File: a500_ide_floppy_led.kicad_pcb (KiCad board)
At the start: 2 copper layers, 21.3 x 11.8 mm, 6 parts, among them J1 Motherboard, J2 Keyboard, J3 ~{IDE_ACTIVITY}, Q1 2N3906

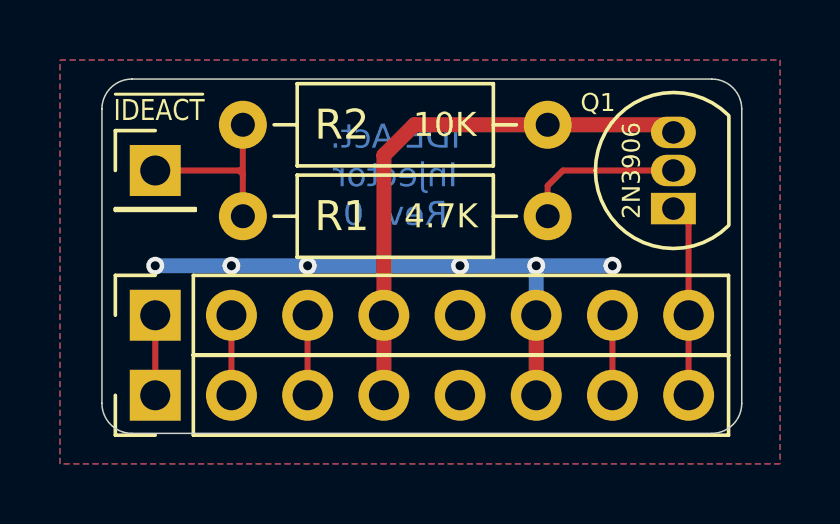
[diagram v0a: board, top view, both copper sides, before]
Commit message: Slightly shrink the board
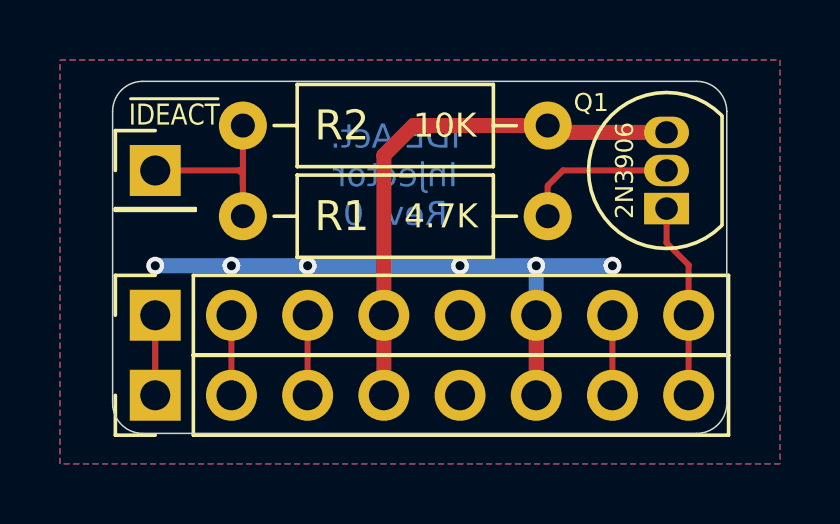
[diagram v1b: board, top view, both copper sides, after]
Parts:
- moved Q1 0.23 mm to (119.3, 25.3)
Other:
- board size 21.3 x 11.8 mm -> 20.5 x 11.7 mm
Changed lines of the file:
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@@
 	(footprint "Resistor_THT:R_Axial_DIN0207_L6.3mm_D2.5mm_P10.16mm_Horizontal"
 		(layer "F.Cu")
-		(at 115.316 22.479 180)
+		(at 115.316 22.5044 180)
 		(descr "Resistor, Axial_DIN0207 series, Axial, Horizontal, pin pitch=10.16mm, 0.25W = 1/4W, length*diameter=6.3*2.5mm^2, http://cdn-reichelt.de/documents/datenblatt/B400/1_4W%23YAG.pdf")
 		(tags "Resistor Axial_DIN0207 series Axial Horizontal pin pitch 10.16mm 0.25W = 1/4W length 6.3mm diameter 2.5mm")
@@
 	(footprint "Package_TO_SOT_THT:TO-92_Inline"
 		(layer "F.Cu")
-		(at 119.507 25.273 90)
+		(at 119.2784 25.273 90)
 		(descr "TO-92 leads in-line, narrow, oval pads, drill 0.75mm (see NXP sot054_po.pdf)")
 		(tags "to-92 sc-43 sc-43a sot54 PA33 transistor")
@@
 		)
 	)
-	(gr_line
-		(start 100.457 31.766)
-		(end 100.457 21.955)
+	(gr_arc
+		(start 120.285 21.0312)
+		(mid 120.992107 21.324093)
+		(end 121.285 22.0312)
 		(stroke
 			(width 0.05)
@@
 	)
 	(gr_line
-		(start 101.457 20.955)
-		(end 120.785 20.955)
+		(start 100.8142 31.766)
+		(end 100.8142 22.0312)
 		(stroke
 			(width 0.05)
@@
 	)
 	(gr_arc
-		(start 120.785 20.955)
-		(mid 121.492107 21.247893)
-		(end 121.785 21.955)
+		(start 100.8142 22.0312)
+		(mid 101.107093 21.324093)
+		(end 101.8142 21.0312)
 		(stroke
 			(width 0.05)
@@
 		(layer "Edge.Cuts")
 	)
-	(gr_arc
-		(start 101.457 32.766)
-		(mid 100.749893 32.473107)
-		(end 100.457 31.766)
+	(gr_line
+		(start 121.285 22.0312)
+		(end 121.285 31.766)
 		(stroke
 			(width 0.05)
@@
 		(layer "Edge.Cuts")
 	)
-	(gr_arc
-		(start 121.785 31.766)
-		(mid 121.492107 32.473107)
-		(end 120.785 32.766)
+	(gr_line
+		(start 101.8142 21.0312)
+		(end 120.285 21.0312)
 		(stroke
 			(width 0.05)
@@
 		(layer "Edge.Cuts")
 	)
-	(gr_line
-		(start 120.785 32.766)
-		(end 101.457 32.766)
+	(gr_arc
+		(start 101.8142 32.766)
+		(mid 101.107093 32.473107)
+		(end 100.8142 31.766)
 		(stroke
 			(width 0.05)
@@
 		(layer "Edge.Cuts")
 	)
-	(gr_arc
-		(start 100.457 21.955)
-		(mid 100.749893 21.247893)
-		(end 101.457 20.955)
+	(gr_line
+		(start 120.285 32.766)
+		(end 101.8142 32.766)
 		(stroke
 			(width 0.05)
@@
 		(layer "Edge.Cuts")
 	)
-	(gr_line
-		(start 121.785 21.955)
-		(end 121.785 31.766)
+	(gr_arc
+		(start 121.285 31.766)
+		(mid 120.992107 32.473107)
+		(end 120.285 32.766)
 		(stroke
 			(width 0.05)
@@
 	)
 	(gr_text "~{IDEACT}"
-		(at 102.362 21.9964 0)
+		(at 102.87 22.1488 0)
 		(layer "F.SilkS")
 		(effects
@@
 	)
 	(segment
-		(start 109.855 23.495)
-		(end 110.871 22.479)
+		(start 119.2784 22.733)
+		(end 115.5446 22.733)
 		(width 0.5)
 		(layer "F.Cu")
@@
 	)
 	(segment
-		(start 110.871 22.479)
-		(end 115.316 22.479)
+		(start 115.316 22.5044)
+		(end 110.8456 22.5044)
 		(width 0.5)
 		(layer "F.Cu")
@@
 	)
 	(segment
-		(start 115.316 22.479)
-		(end 119.253 22.479)
+		(start 119.0244 22.479)
+		(end 119.2784 22.733)
+		(width 0.5)
+		(layer "F.Cu")
+		(net 1)
+	)
+	(segment
+		(start 110.8456 22.5044)
+		(end 109.855 23.495)
 		(width 0.5)
 		(layer "F.Cu")
@@
 		(start 109.855 28.829)
 		(end 109.855 23.495)
+		(width 0.5)
+		(layer "F.Cu")
+		(net 1)
+	)
+	(segment
+		(start 115.5446 22.733)
+		(end 115.316 22.5044)
 		(width 0.5)
 		(layer "F.Cu")
@@
 	)
 	(segment
-		(start 120.015 25.781)
-		(end 119.507 25.273)
-		(width 0.2)
-		(layer "F.Cu")
-		(net 8)
-	)
-	(segment
 		(start 120.015 28.829)
-		(end 120.015 25.781)
+		(end 120.015 27.1526)
 		(width 0.2)
 		(layer "F.Cu")
@@
 	)
 	(segment
+		(start 119.2784 26.416)
+		(end 119.2784 25.273)
+		(width 0.2)
+		(layer "F.Cu")
+		(net 8)
+	)
+	(segment
+		(start 120.015 27.1526)
+		(end 119.2784 26.416)
+		(width 0.2)
+		(layer "F.Cu")
+		(net 8)
+	)
+	(segment
+		(start 105.156 22.5044)
+		(end 105.156 24.4856)
+		(width 0.2)
+		(layer "F.Cu")
+		(net 10)
+	)
+	(segment
+		(start 105.156 24.4856)
+		(end 105.156 25.527)
+		(width 0.2)
+		(layer "F.Cu")
+		(net 10)
+	)
+	(segment
 		(start 105.156 24.13)
-		(end 105.156 25.527)
+		(end 105.156 24.4856)
 		(width 0.2)
 		(layer "F.Cu")
@@
 	)
 	(segment
-		(start 105.156 22.479)
-		(end 105.156 24.13)
-		(width 0.2)
-		(layer "F.Cu")
-		(net 10)
-	)
-	(segment
 		(start 115.316 24.511)
 		(end 115.316 25.527)
@@
 	)
 	(segment
-		(start 119.507 24.003)
-		(end 115.824 24.003)
-		(width 0.2)
-		(layer "F.Cu")
+		(start 115.824 24.003)
+		(end 119.2784 24.003)
+		(width 0.2)
+		(layer "F.Cu")
